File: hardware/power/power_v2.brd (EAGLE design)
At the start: 92 x 92 mm, 61 parts, among them J1 FASTON1289_ST, J2 FASTON1289_ST, J3 12v, J4 5v, J5 XT30PW-F, J6 XT30PW-F, J7 XT30PW-F, J8 XT30PW-F, Q1 MMBT5401L, Q2 PSMN1R0-40YSH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

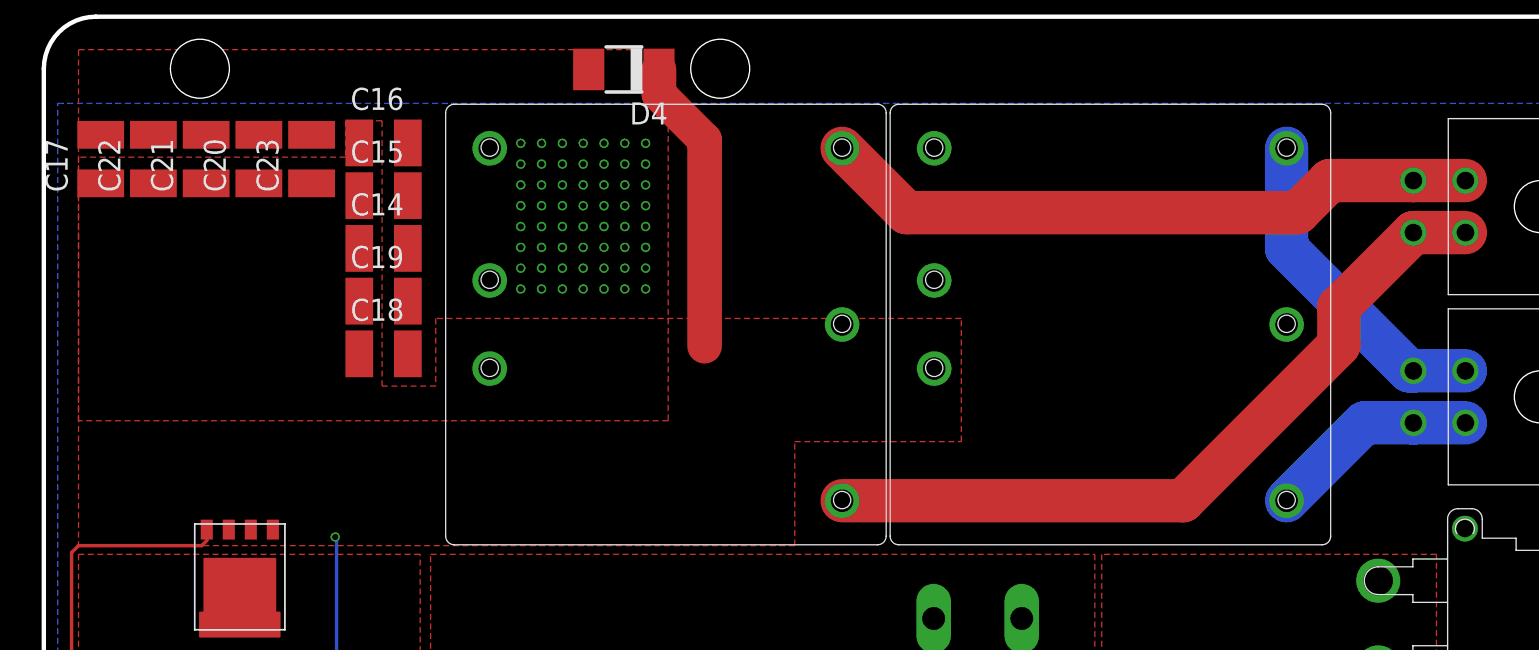
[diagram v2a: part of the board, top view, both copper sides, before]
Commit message: Separated DC converters
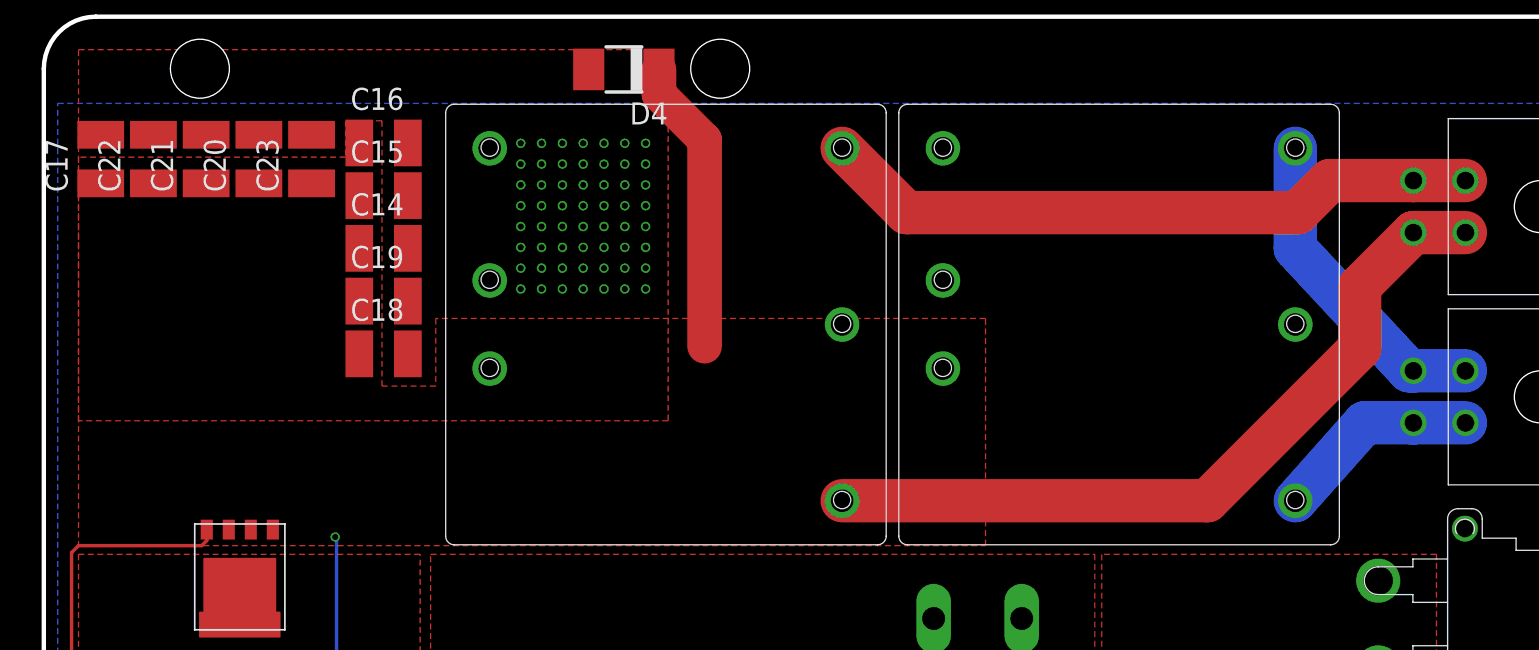
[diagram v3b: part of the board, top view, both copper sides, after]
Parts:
- moved U1 0.50 mm to (62.0, 74.2)
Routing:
- net +12VOUT: track 43.6 -> 44.4 mm
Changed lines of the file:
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@@
 </layers>
 <board>
-<fusionsync huburn="a.YnVzaW5lc3M6Z21haWwyMjE5MTc" projecturn="a.YnVzaW5lc3M6Z21haWwyMjE5MTcjMjAxOTA2MjkyMDE0MTU5NzY" f3durn="urn:adsk.wipprod:dm.lineage:MB3VqYkNRX6Sa_ecpPTqbA" pcbguid="9dcfff74-9686-4bdf-a14e-dd144a326308" lastpulledtime="2020-01-18T04:37:27Z" lastsyncedchangeguid="949c5408-da32-ad4a-ba52-90464d57dd80"/>
+<fusionsync huburn="a.YnVzaW5lc3M6Z21haWwyMjE5MTc" projecturn="a.YnVzaW5lc3M6Z21haWwyMjE5MTcjMjAxOTA2MjkyMDE0MTU5NzY" f3durn="urn:adsk.wipprod:dm.lineage:MB3VqYkNRX6Sa_ecpPTqbA" pcbguid="9dcfff74-9686-4bdf-a14e-dd144a326308" lastpulledtime="2020-01-18T04:37:27Z" lastsyncedchangeguid="d8272236-d454-ed0b-d109-326f528a605c"/>
 <plain>
 <hole x="39" y="89" drill="3.4"/>
@@
 <element name="J3" library="timlib" library_urn="urn:adsk.eagle:library:16152524" package="MOLEX_4_RA" package3d_urn="urn:adsk.eagle:package:16152611/3" value="12v" x="86.29" y="81.05" smashed="yes" rot="R90"/>
 <element name="J4" library="timlib" library_urn="urn:adsk.eagle:library:16152524" package="MOLEX_4_RA" package3d_urn="urn:adsk.eagle:package:16152611/3" value="5v" x="86.29" y="70.08" smashed="yes" rot="R90"/>
-<element name="U1" library="timlib" library_urn="urn:adsk.eagle:library:16152524" package="PDQ30-D" package3d_urn="urn:adsk.eagle:package:16187995/3" value="PDQ30-Q24-S5-D" x="61.5" y="74.25" smashed="yes" rot="R90"/>
+<element name="U1" library="timlib" library_urn="urn:adsk.eagle:library:16152524" package="PDQ30-D" package3d_urn="urn:adsk.eagle:package:16187995/3" value="PDQ30-Q24-S5-D" x="62" y="74.25" smashed="yes" rot="R90"/>
 <element name="U2" library="timlib" library_urn="urn:adsk.eagle:library:16152524" package="PDQ30-D" package3d_urn="urn:adsk.eagle:package:16187995/3" value="PDQ30-Q24-S12-D" x="35.87" y="74.25" smashed="yes" rot="R90"/>
 <element name="U$26" library="timlib" library_urn="urn:adsk.eagle:library:16152524" package="M80-8420242" package3d_urn="urn:adsk.eagle:package:16399492/3" value="2-PIN" x="28.58" y="11" smashed="yes"/>
@@
 <contactref element="J4" pad="CIRCUIT2"/>
 <contactref element="J4" pad="CIRCUIT4"/>
-<wire x1="71.66" y1="64.09" x2="76.15" y2="68.58" width="2.5" layer="16"/>
+<wire x1="72.16" y1="64.09" x2="76.15" y2="68.58" width="2.5" layer="16"/>
 <wire x1="76.15" y1="68.58" x2="78.97" y2="68.58" width="2.5" layer="16"/>
 <wire x1="78.97" y1="68.58" x2="81.972" y2="68.58" width="2.5" layer="16"/>
@@
 <contactref element="J3" pad="CIRCUIT2"/>
 <contactref element="U2" pad="P$3"/>
-<wire x1="46.03" y1="64.09" x2="65.69" y2="64.09" width="2.5" layer="1"/>
-<wire x1="78.97" y1="79.55" x2="74.67" y2="75.25" width="2.5" layer="1"/>
-<wire x1="74.67" y1="75.25" x2="74.67" y2="73.07" width="2.5" layer="1"/>
-<wire x1="74.67" y1="73.07" x2="65.69" y2="64.09" width="2.5" layer="1"/>
+<wire x1="46.03" y1="64.09" x2="67.09" y2="64.09" width="2.5" layer="1"/>
+<wire x1="78.97" y1="79.55" x2="75.87" y2="76.45" width="2.5" layer="1"/>
+<wire x1="75.87" y1="76.45" x2="75.87" y2="72.87" width="2.5" layer="1"/>
+<wire x1="75.87" y1="72.87" x2="67.09" y2="64.09" width="2.5" layer="1"/>
 <wire x1="81.972" y1="79.55" x2="78.97" y2="79.55" width="2.5" layer="1"/>
 </signal>
@@
 <contactref element="J4" pad="CIRCUIT3"/>
 <contactref element="U1" pad="P$5"/>
-<wire x1="71.66" y1="84.41" x2="71.66" y2="78.64" width="2.5" layer="16"/>
+<wire x1="72.16" y1="84.41" x2="72.16" y2="78.64" width="2.5" layer="16"/>
 <wire x1="78.97" y1="71.58" x2="78.72" y2="71.58" width="2.5" layer="16"/>
-<wire x1="78.72" y1="71.58" x2="71.66" y2="78.64" width="2.5" layer="16"/>
+<wire x1="78.72" y1="71.58" x2="72.16" y2="78.64" width="2.5" layer="16"/>
 <wire x1="78.97" y1="71.58" x2="81.97" y2="71.58" width="2.5" layer="16"/>
 </signal>
@@
 <polygon width="0.1524" layer="1" isolate="0.3" thermals="no">
 <vertex x="2" y="61.5"/>
-<vertex x="43.3" y="61.5"/>
-<vertex x="43.3" y="67.5"/>
-<vertex x="52.9" y="67.5"/>
-<vertex x="52.9" y="74.6"/>
+<vertex x="54.3" y="61.5"/>
+<vertex x="54.3" y="74.6"/>
 <vertex x="22.6" y="74.6"/>
 <vertex x="22.6" y="70.7"/>
